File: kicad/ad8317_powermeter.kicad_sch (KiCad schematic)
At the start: 0 parts

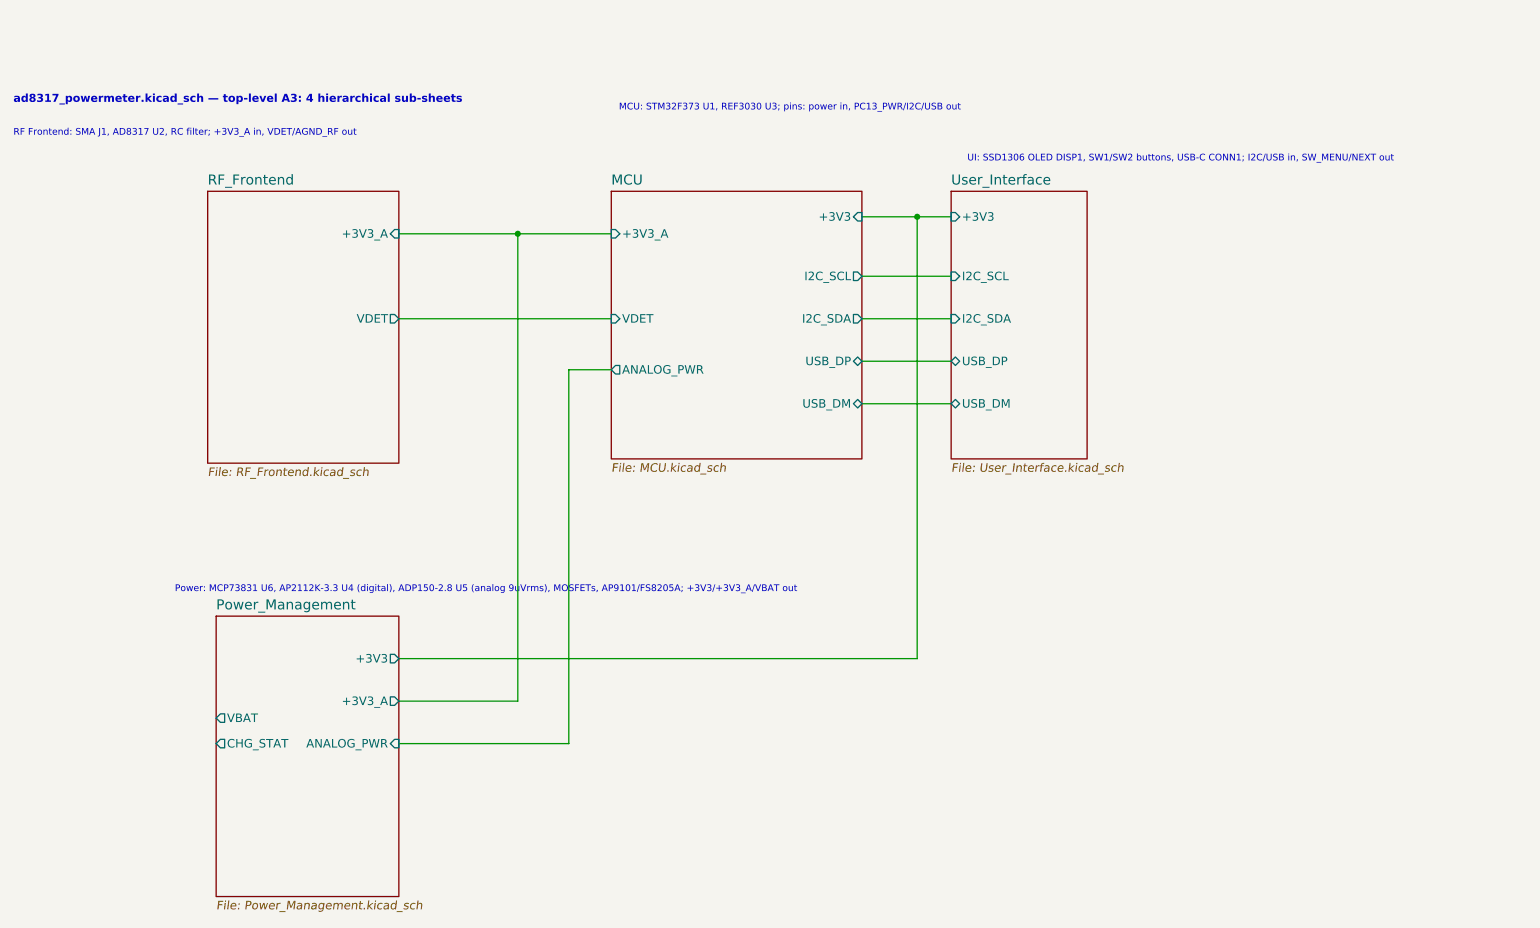
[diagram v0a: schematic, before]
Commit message: Add calibration scripts, documentation, simulation tools, and KiCad updates
- cal/calibration.py: 3-phase RF linearity calibration (29 freq, 28 power steps,
  1 MHz–10 GHz, direct generator→DUT, no attenuator, NRP sensor 0.01 dBm precision)
- cal/temp_calibration.py: temperature calibration via Vötsch chamber (16–40°C,
  Vötsch SIMSERV TCP driver, tracking generator source, outputs TEMP_COEFF_DB_PER_C[])
- cal/results/: dry-run calibration tables (.h/.json), figures, PDF reports
- doc/: ADC signal path analysis, calibration procedure (3-phase), lab optimisation
  guide updated for 1 MHz–10 GHz range and temperature correction firmware formula
- doc/diagrams/: PlantUML/Mermaid source + rendered PNGs for pipeline, firmware,
  and RF signal chain architectures
- sim/ltpwr_to_touchstone.py: LTpowerAnalyzer Z(f) → Touchstone S1P + Z1P via
  scikit-rf for SIwave PI-AC Decoupling Optimization DC/DC source impedance import
- sim/Measured_source_impedance.txt/.s1p/.z1p: DC/DC output impedance measurement
  and converted Touchstone files (100 Hz–10 MHz, 201 points)
- kicad/: updated schematics (MCU, power management, RF frontend, UI) and PCB layout
- kicad/fixture-rev_A/: test fixture DXF drawings
- lib/: Würth 744231091 datasheet, Hammond 1590A board outline footprint
- pp_3d_printer_setup_spec.md, pp_horn_antenna_manufacturing_spec.md: process specs

Co-Authored-By: Claude Sonnet 4.6 <noreply@anthropic.com>
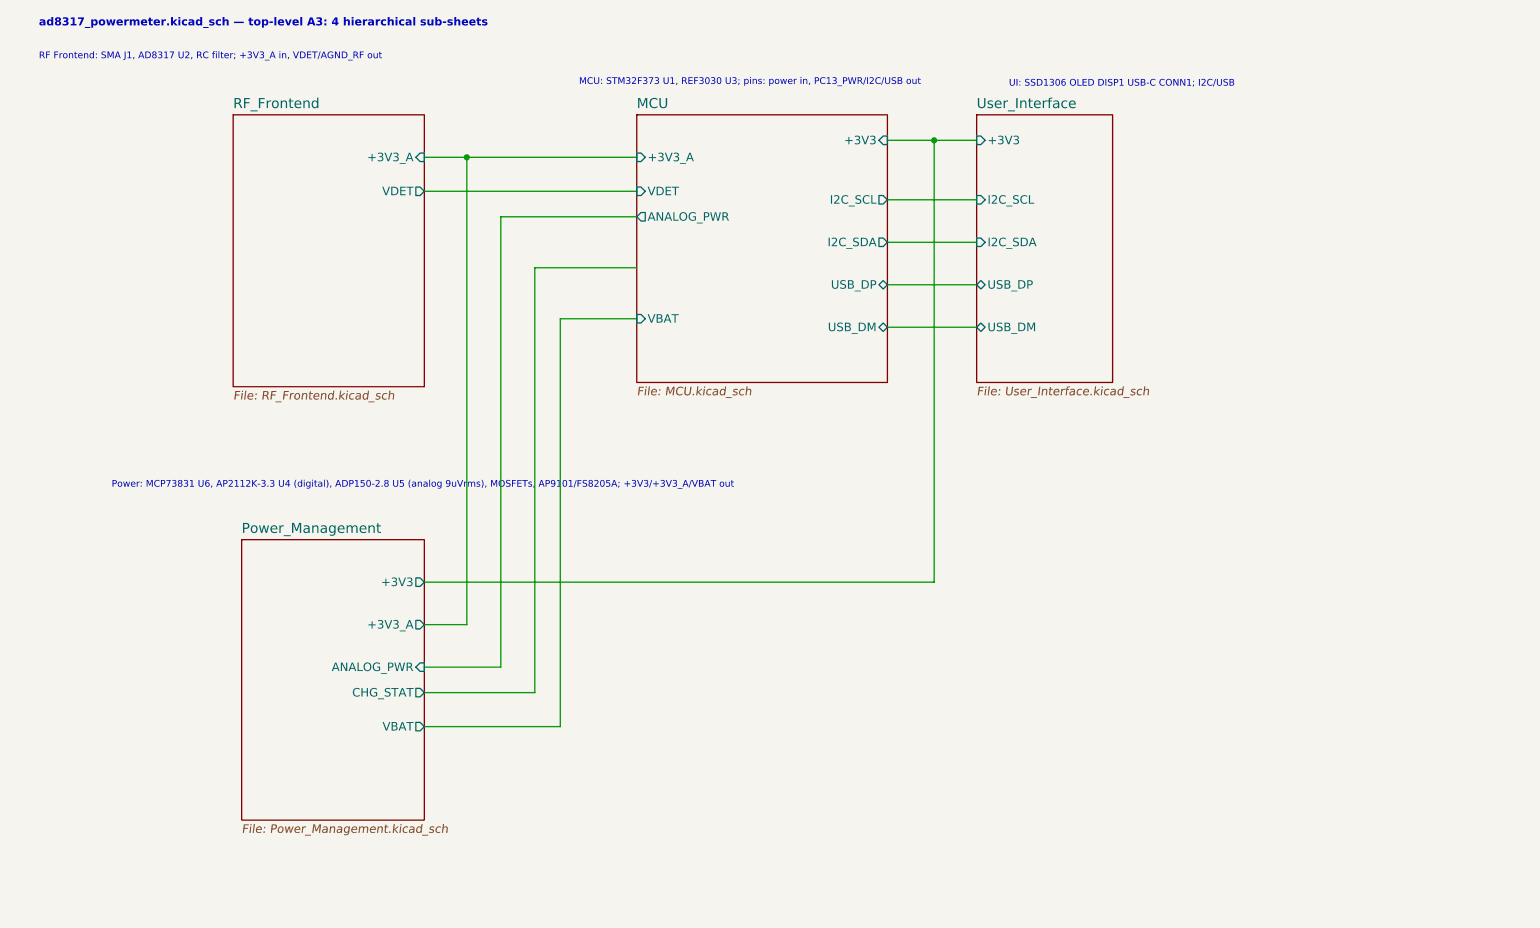
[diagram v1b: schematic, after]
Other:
- sheet MCU ports: added VBAT; removed none
- note added: "UI: SSD1306 OLED DISP1 USB-C CONN1; I2C/USB"
- note removed: "UI: SSD1306 OLED DISP1, SW1/SW2 buttons, USB-C CONN1; I2C/USB in, SW_MENU/NEXT out"
